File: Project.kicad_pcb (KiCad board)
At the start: 2 copper layers, 25 parts, among them J1 Screw_Terminal_01x02, J2 Screw_Terminal_01x02, J3 Conn_01x04_Socket, Q1 BT136-500, U1 AMS1117-3.3, U2 ESP32-WROOM-32, U3 MOC3021M, U4 MCT2E

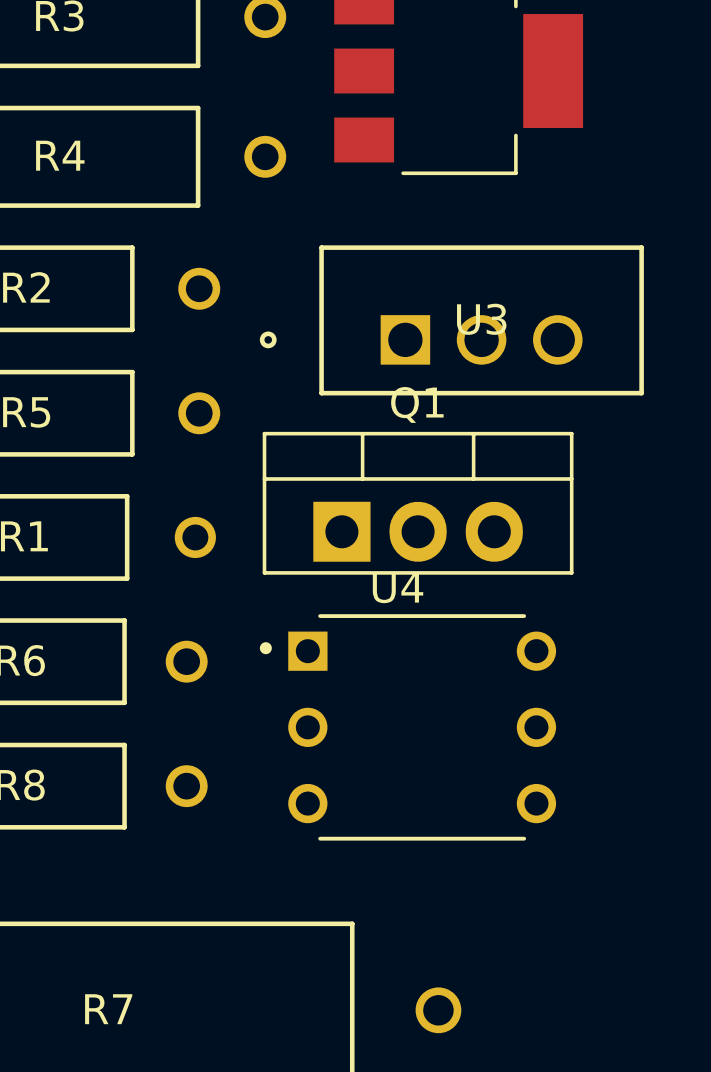
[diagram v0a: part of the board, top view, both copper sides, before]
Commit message: Added 3d models
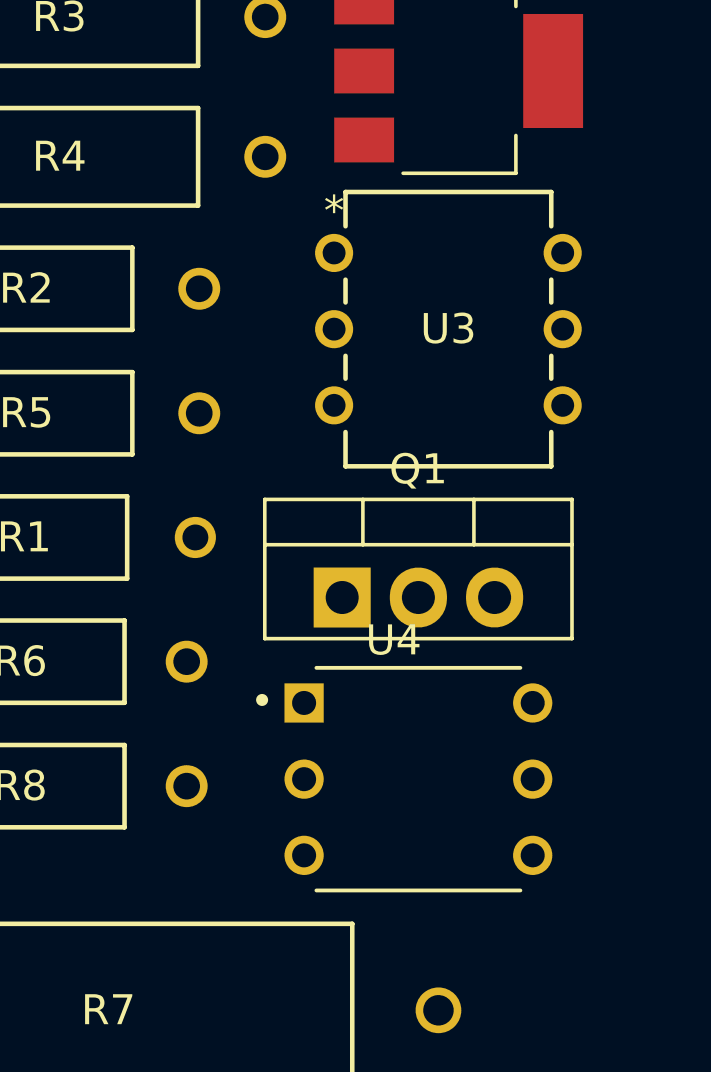
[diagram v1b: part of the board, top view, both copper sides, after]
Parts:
- U3: footprint Triac_BTA16:TO-220AB_STM -> MOC3021M:PDIP6_BX_ONS
- moved U3 3.75 mm to (160.2, 82.5)
- moved Q1 2.19 mm to (160.5, 93.9)
- moved U4 1.73 mm to (163.0, 100.0)

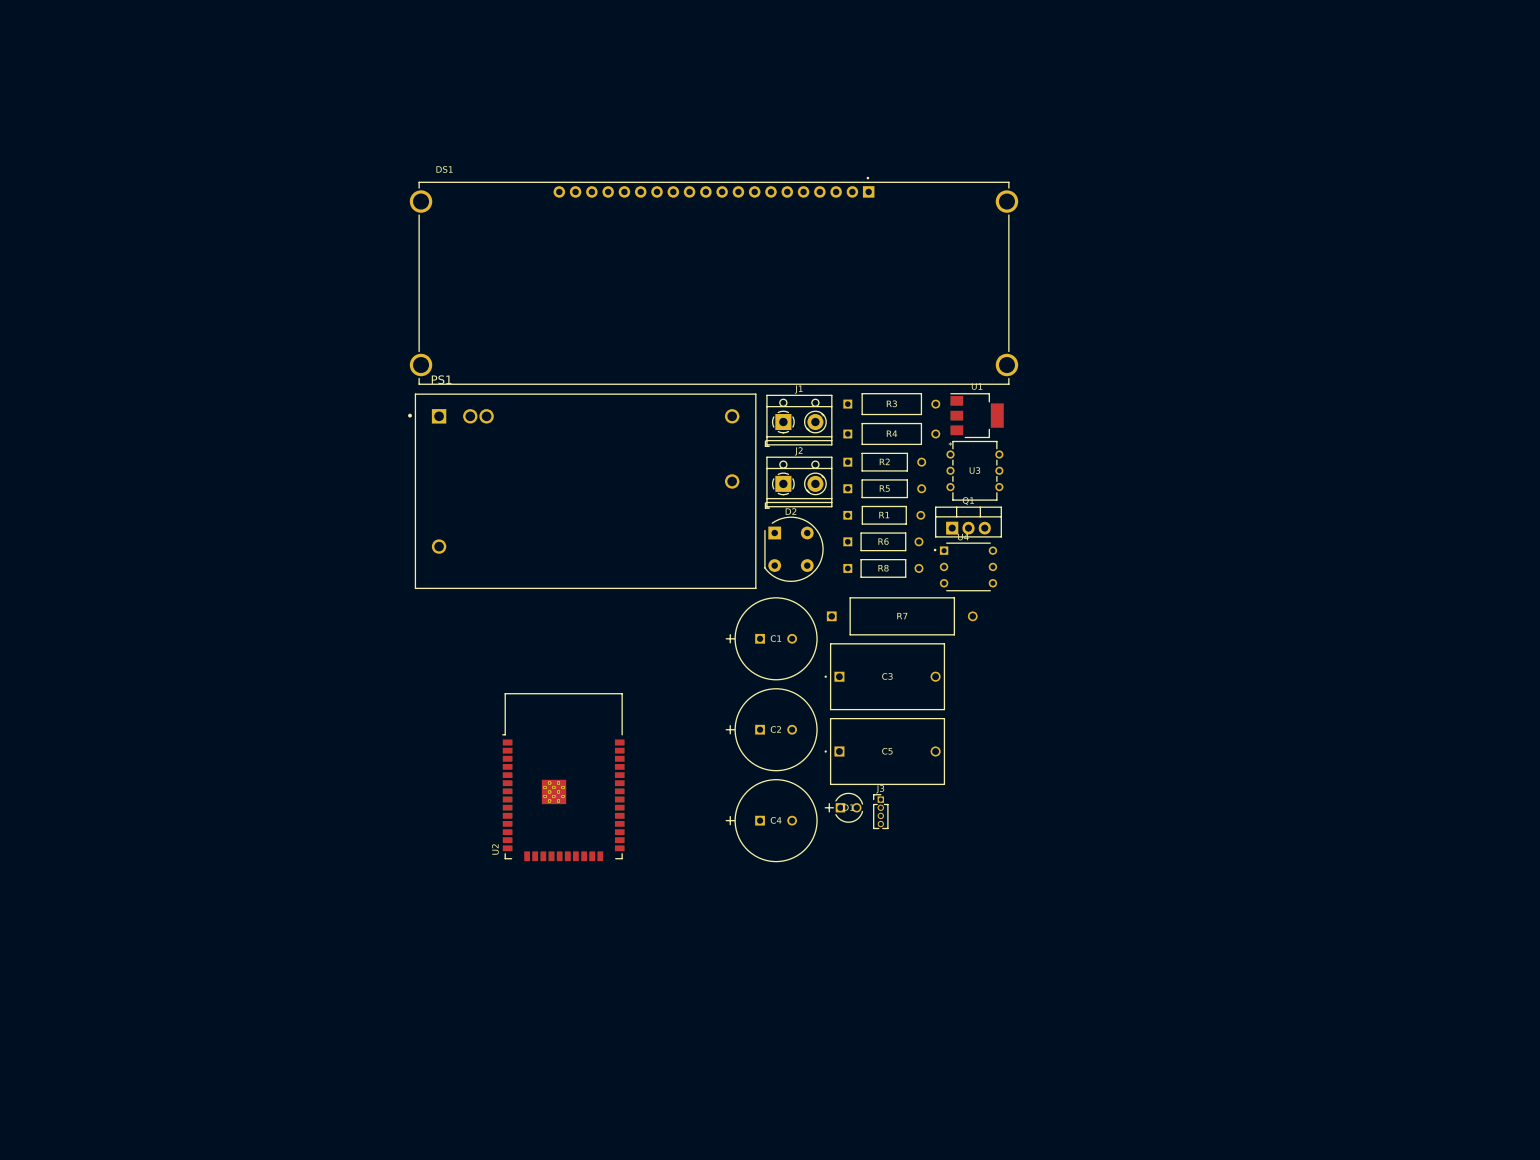
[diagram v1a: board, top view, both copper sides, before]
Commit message: Added footprints
To-do finish list:
*Add connection LED disp<->MCU
*Assign footprints to:
Capacitors: 10,12,13,14,16,18,19,20;
Jumper JP1;
Mikrophone MK1;
*Assign 3d models;
*PCB design.
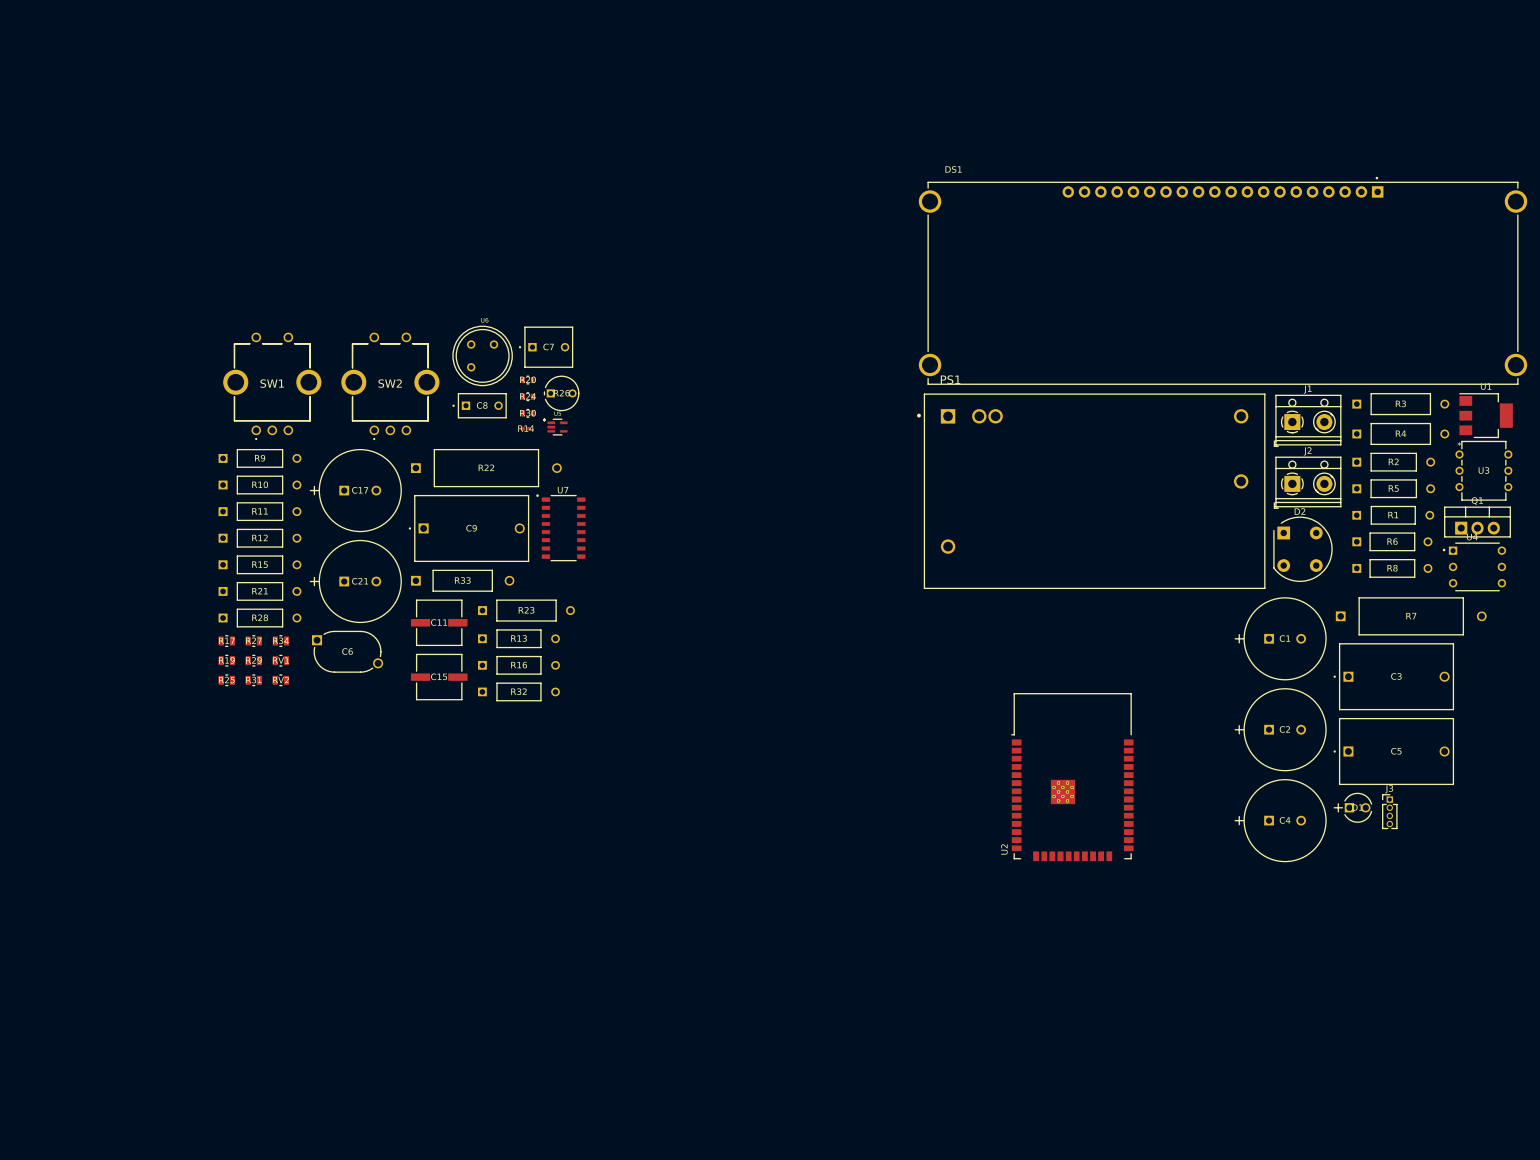
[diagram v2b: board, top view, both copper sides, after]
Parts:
- added C11: 47u, Capacitor_47uF:CAP_EEFK_D_PAN, F.Cu at (80.4, 108.7)
- added C15: 47u, Capacitor_47uF:CAP_EEFK_D_PAN, F.Cu at (80.4, 117.2)
- added C17: 22u, Capacitor_22uF:PCAP_125x25_PAN, F.Cu at (65.6, 88.1)
- added C21: 22u, Capacitor_22uF:PCAP_125x25_PAN, F.Cu at (65.6, 102.3)
- added C6: 100p, Capacitor_100p:564R60GAT10_VIS, F.Cu at (66.1, 113.2)
- added C7: 1u, Capacitor_1uF:CAP_BFC237012105_VIS, F.Cu at (95.0, 65.7)
- added C8: 0.01u, Capacitor_0_01uF:CAP_BFC237035223_VIS, F.Cu at (84.6, 74.8)
- added C9: 0.1u, Capacitor_0_1uF:CAP_BFC233814104_VIS, F.Cu at (78.0, 94.0)
- added R10: 10k, Resistor_10k:RES_CFR25_TYCO_TYC, F.Cu at (46.7, 87.2)
- added R11: 10k, Resistor_10k:RES_CFR25_TYCO_TYC, F.Cu at (46.7, 91.4)
- added R12: 10k, Resistor_10k:RES_CFR25_TYCO_TYC, F.Cu at (46.7, 95.5)
- added R13: 2k, Resistor_2k:RES_TYCO_YR1_TYC, F.Cu at (87.2, 111.2)
- added R14: 100k, Resistor_100k:RES0402_CRG_TYCO_TYC, F.Cu at (94.0, 78.5)
- added R15: 10k, Resistor_10k:RES_CFR25_TYCO_TYC, F.Cu at (46.7, 99.7)
- added R16: 2k, Resistor_2k:RES_TYCO_YR1_TYC, F.Cu at (87.2, 115.4)
- added R17: 1M, Resistor_1M:RES0805_CRG_TYCO_TYC, F.Cu at (47.3, 111.6)
- added R19: 1M, Resistor_1M:RES0805_CRG_TYCO_TYC, F.Cu at (47.3, 114.6)
- added R20: 18k, Resistor_18k:RES0603_CRG_TYCO_TYC, F.Cu at (94.3, 70.8)
- added R21: 10k, Resistor_10k:RES_CFR25_TYCO_TYC, F.Cu at (46.7, 103.8)
- added R22: 1K, Resistor_1k:RES_CFR200_TYCO_TYC, F.Cu at (76.8, 84.6)
- added R23: 47k, Resistor_47k:RES_CFR50_TYCO_TYC, F.Cu at (87.2, 106.8)
- added R24: 18k, Resistor_18k:RES0603_CRG_TYCO_TYC, F.Cu at (94.3, 73.4)
- added R25: 1M, Resistor_1M:RES0805_CRG_TYCO_TYC, F.Cu at (47.3, 117.7)
- added R26: R_Photo, Photoresistor:LDR1_NTE, F.Cu at (97.8, 72.9)
- added R27: 1M, Resistor_1M:RES0805_CRG_TYCO_TYC, F.Cu at (51.5, 111.6)
- added R28: 10k, Resistor_10k:RES_CFR25_TYCO_TYC, F.Cu at (46.7, 108.0)
- added R29: 1M, Resistor_1M:RES0805_CRG_TYCO_TYC, F.Cu at (51.5, 114.6)
- added R30: 18k, Resistor_18k:RES0603_CRG_TYCO_TYC, F.Cu at (94.3, 76.0)
- added R31: 1M, Resistor_1M:RES0805_CRG_TYCO_TYC, F.Cu at (51.5, 117.7)
- added R32: 2k, Resistor_2k:RES_TYCO_YR1_TYC, F.Cu at (87.2, 119.5)
- added R33: 6.8k, Resistor_6_8k:RES_ROX1S_TYCO_TYC, F.Cu at (76.8, 102.2)
- added R34: 470k, Resistor_470k:RES0805_CRG_TYCO_TYC, F.Cu at (55.7, 111.6)
- added R9: 10k, Resistor_10k:RES_CFR25_TYCO_TYC, F.Cu at (46.7, 83.1)
- added RV1: 1M, Resistor_1M:RES0805_CRG_TYCO_TYC, F.Cu at (55.7, 114.6)
- added RV2: 1M, Resistor_1M:RES0805_CRG_TYCO_TYC, F.Cu at (55.7, 117.7)
- added SW1: PEC11H, PEC11H_RE:PEC11H4025FS0016, F.Cu at (51.9, 78.7)
- added SW2: PEC11H, PEC11H_RE:PEC11H4025FS0016, F.Cu at (70.3, 78.7)
- added U5: MAX4466EXK, MAX4466EXK:SOT65P210X110-5N, F.Cu at (98.9, 78.2)
- added U6: RE200B, DIP-MOTION_POSITION-LHI778_3P-D8.1MM_:SNR3-D8.1XH4.2MM, F.Cu at (87.2, 67.1)
- added U7: BISS0001, BISS0001:SOIC127P600X180-16N, F.Cu at (99.8, 93.9)
- moved C1 79.4 mm to (209.9, 111.2)
- moved C2 79.4 mm to (209.9, 125.4)
- moved C4 79.4 mm to (209.9, 139.6)
- moved J1 79.4 mm to (213.5, 77.4)
- moved J2 79.4 mm to (213.5, 87.0)
- moved J3 79.4 mm to (228.7, 136.3)
- moved PS1 79.4 mm to (182.7, 88.2)
- moved Q1 79.4 mm to (239.9, 93.9)
- moved R1 79.4 mm to (223.6, 91.9)
- moved R2 79.4 mm to (223.6, 83.7)
- moved R3 79.4 mm to (223.6, 74.6)
- moved R4 79.4 mm to (223.6, 79.3)
- moved R5 79.4 mm to (223.6, 87.8)
- moved R6 79.4 mm to (223.6, 96.1)
- moved R7 79.4 mm to (221.1, 107.7)
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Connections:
- U2 pad 13: unconnected-(U2-IO14-Pad13) -> SW1
- U2 pad 14: unconnected-(U2-IO12-Pad14) -> ENC1_2
- U2 pad 16: unconnected-(U2-IO13-Pad16) -> ENC1_1
- U2 pad 23: unconnected-(U2-IO15-Pad23) -> ENC2_2
- U2 pad 26: unconnected-(U2-IO4-Pad26) -> TRIAC_1
- U2 pad 27: unconnected-(U2-IO16-Pad27) -> ENC2_1
- U2 pad 28: unconnected-(U2-IO17-Pad28) -> SW2
- U2 pad 29: unconnected-(U2-IO5-Pad29) -> ZC
- U2 pad 30: unconnected-(U2-IO18-Pad30) -> MIC
- U2 pad 31: unconnected-(U2-IO19-Pad31) -> PIR_SENS

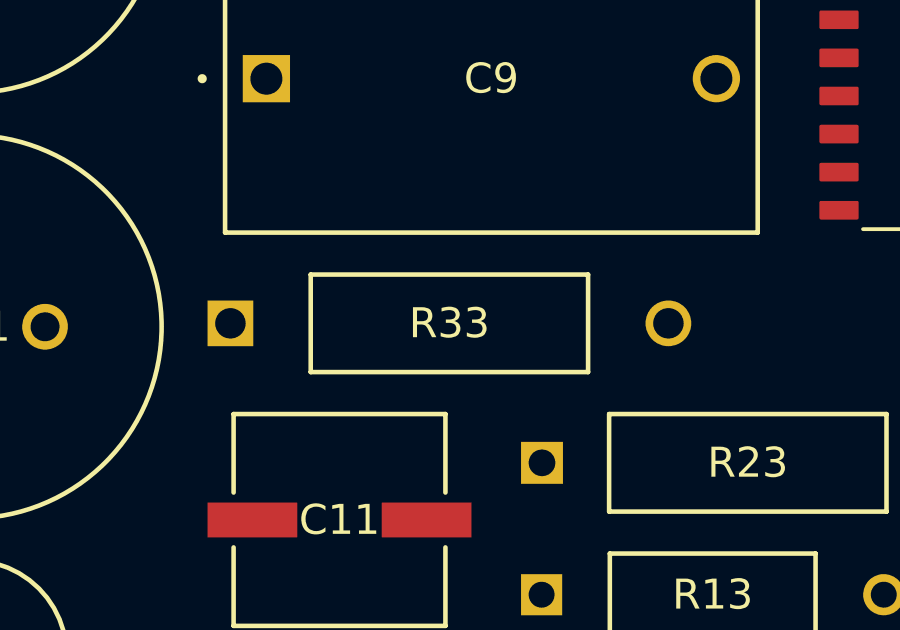
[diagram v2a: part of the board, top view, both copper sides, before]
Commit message: models
several 3d models were added
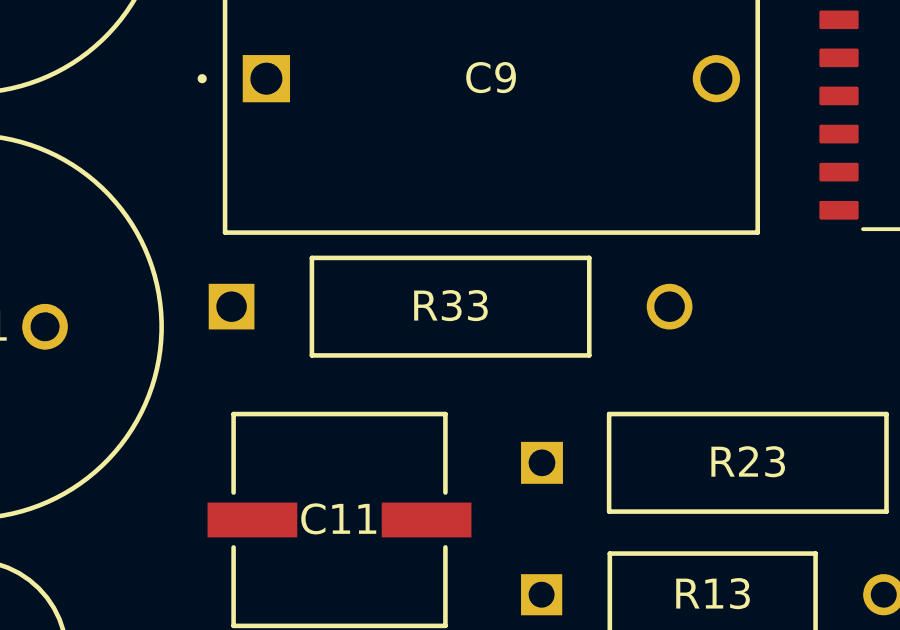
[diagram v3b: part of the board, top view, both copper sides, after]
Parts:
- moved R33 0.56 mm to (76.8, 101.6)
